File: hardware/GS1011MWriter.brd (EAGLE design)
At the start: 54.1 x 56 mm, 15 parts, among them IC1 SN74LVC2G125DCU, IC2 SN74LVC2G125DCU

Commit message: routing
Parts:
- removed $1_6_$, U$2: LED-SPACER, my:LED-SPACER
- removed STANDOFF1, STANDOFF2, STANDOFF3, STANDOFF4: STAND-OFF, my:STAND-OFF
- removed U$1: (no value), logo:IRKIT-LOGO
- moved R3 56.4 mm to (14.3, 16.9), turned to 180 degrees
- moved S1 53.1 mm to (20.9, 18.4), turned to 180 degrees
- moved CN1 47.0 mm to (3.70, 10.4)
- moved R1 41.1 mm to (21.4, 5.40), turned to 90 degrees
- moved R2 35.6 mm to (11.8, 4.80), turned to 90 degrees
- moved IC2 35.1 mm to (16.9, 6.60), turned to 90 degrees
- moved CN2 34.5 mm to (27.8, 9.80), turned to 90 degrees
- moved IC1 33.0 mm to (11.8, 13.6), turned to 270 degrees
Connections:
- net +3V3: now also CN1.1
- net GND: no longer CN1.1
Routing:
- net GND: track 119.4 -> 7.72 mm, vias 87 -> 1
- net +3V3: track 0.00 -> 27.8 mm
- net +5V: track 2.53 -> 29.4 mm, vias 0 -> 1
- net TXD: track 0.00 -> 23.4 mm, vias 0 -> 1
- net RTS#: track 0.00 -> 15.5 mm
- net WIFI_UART0_RX: track 12.9 -> 0.00 mm
- net N$1: track 0.00 -> 10.1 mm
- net WIFI_UART0_RTS: track 15.2 -> 5.70 mm, vias 2 -> 0
- net WIFI_UART0_TX: track 18.4 -> 10.1 mm, vias 2 -> 1
- net WIFI_UART0_CTS: track 14.1 -> 15.5 mm
- net WIFI_UART1_RTS: track 28.4 -> 29.2 mm
- removed copper zone on layer 1, net GND
- removed copper zone on layer 16, net GND
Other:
- board size 54.1 x 56 mm -> 30 x 20 mm
- board text removed: "+5V"
- board text removed: "GND"
- board text removed: "IRKit v1.1.1"

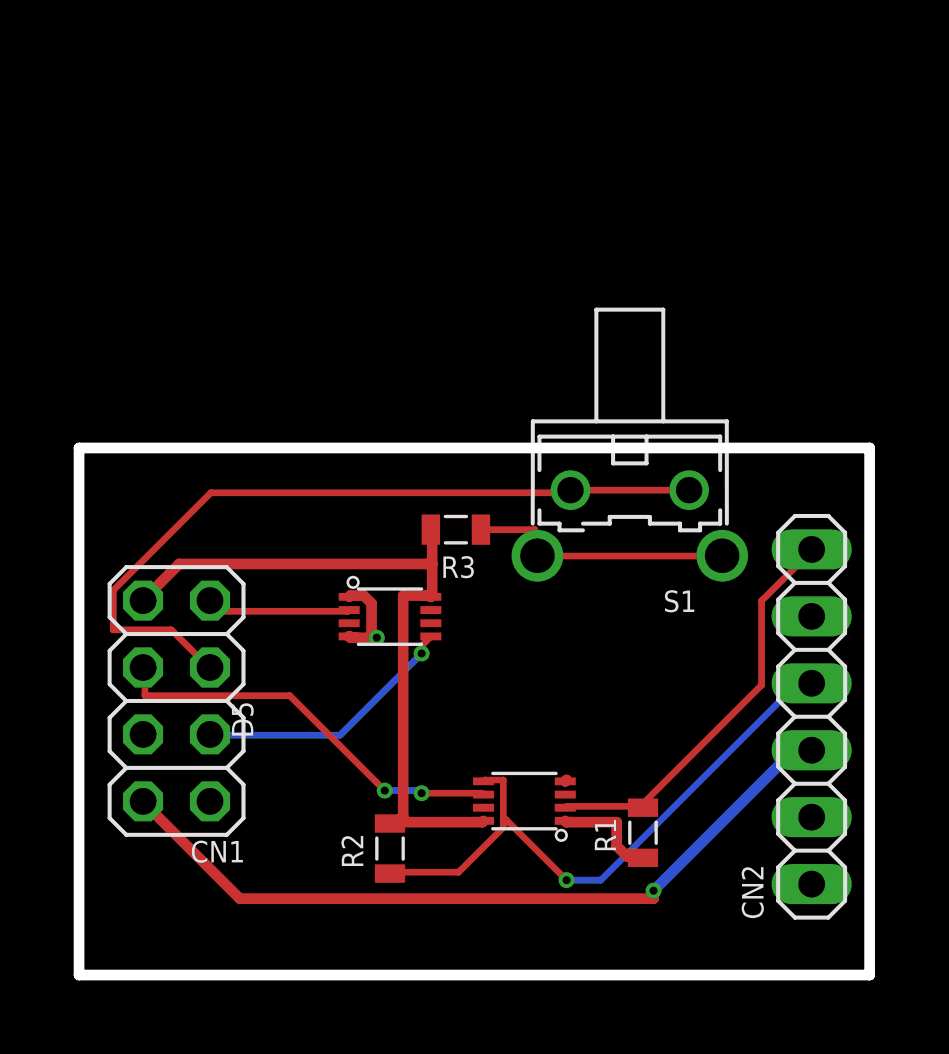
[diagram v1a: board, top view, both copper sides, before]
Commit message: routed GS1011MIPS writer
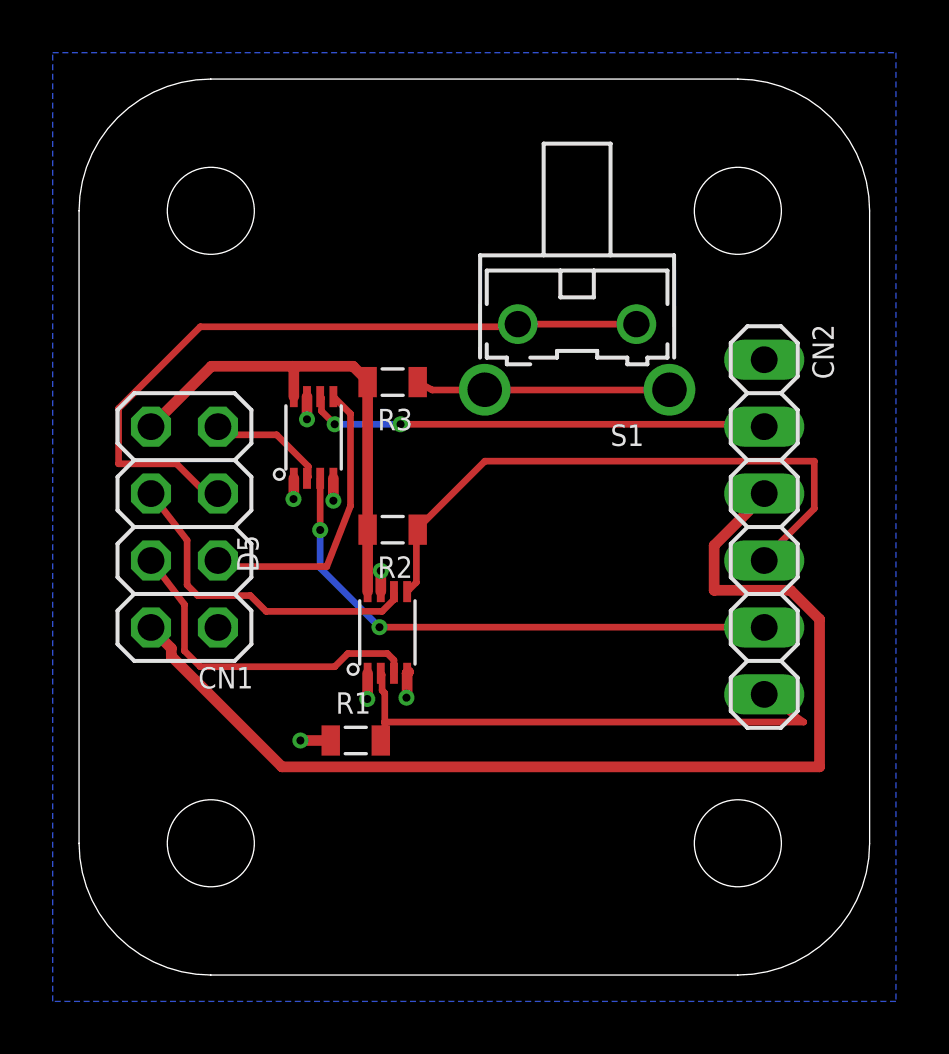
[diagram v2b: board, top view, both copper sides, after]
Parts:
- added STANDOFF1, STANDOFF2, STANDOFF3, STANDOFF4: STAND-OFF, my:STAND-OFF
- moved R2 12.1 mm to (11.9, 16.9), turned to 180 degrees
- moved R1 11.4 mm to (10.5, 8.90), turned to 0 degrees
- moved IC2 8.25 mm to (11.7, 13.0), turned to 0 degrees
- moved CN2 7.42 mm to (26.0, 17.0), turned to 270 degrees
- moved IC1 7.39 mm to (8.90, 20.4), turned to 0 degrees
- moved S1 6.61 mm to (18.9, 24.7)
- moved CN1 6.61 mm to (4.00, 17.0)
- moved R3 6.09 mm to (11.9, 22.5)
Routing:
- net RXD: track 0.00 -> 21.6 mm, vias 0 -> 2
- net CTS#: track 0.00 -> 17.7 mm, vias 0 -> 2
- net WIFI_UART0_RX: track 0.00 -> 12.9 mm
- net +5V: track 29.4 -> 42.3 mm, vias 1 -> 0
- net +3V3: track 27.8 -> 18.6 mm
- net RTS#: track 15.5 -> 20.4 mm
- net WIFI_UART0_CTS: track 15.5 -> 12.7 mm, vias 2 -> 0
- net WIFI_UART1_RTS: track 29.2 -> 27.6 mm
- net WIFI_UART0_TX: track 10.1 -> 11.3 mm, vias 1 -> 0
- net WIFI_UART0_RTS: track 5.70 -> 4.79 mm
- net GND: track 7.72 -> 6.81 mm, vias 1 -> 7
- net TXD: track 23.4 -> 23.2 mm, vias 1 -> 0
- added copper zone on layer 16, net GND
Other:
- board size 30 x 20 mm -> 30 x 34 mm

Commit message: I think I can directly connect TTL-232R-3V3's pins to GS1011MIPS's UART pins
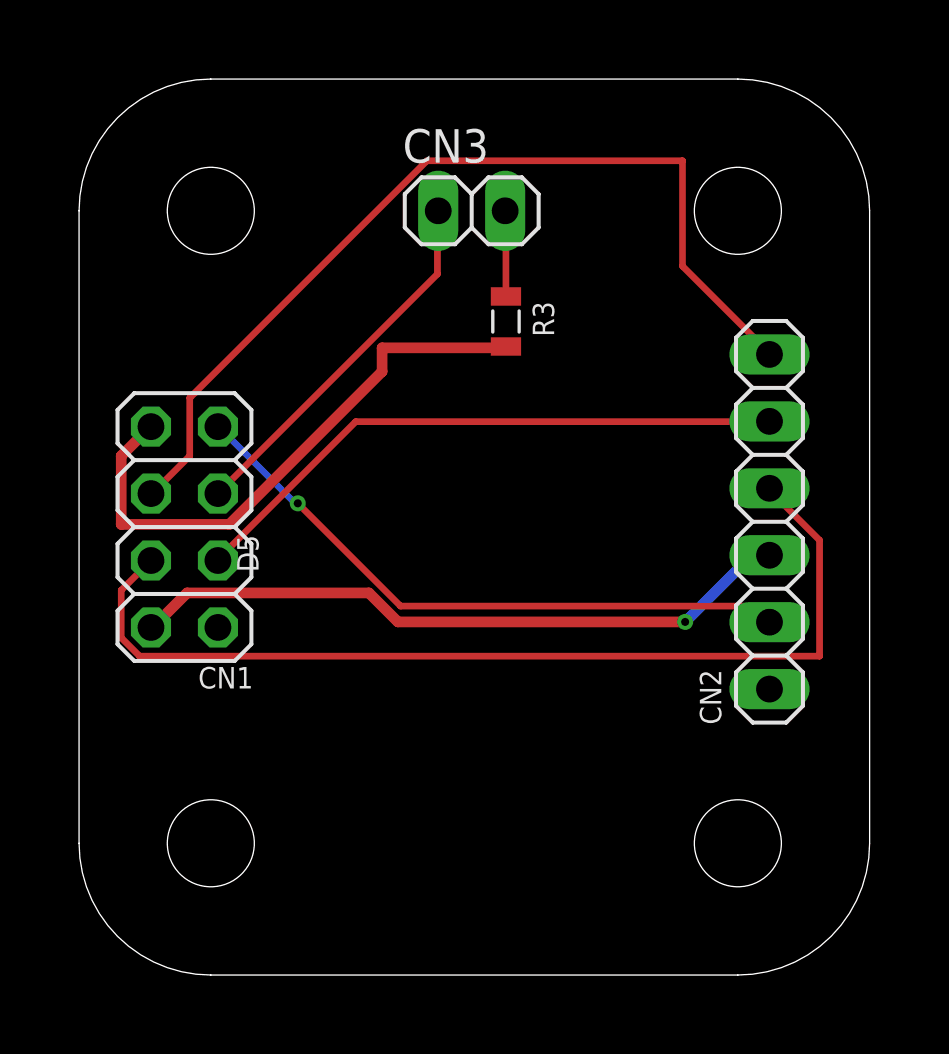
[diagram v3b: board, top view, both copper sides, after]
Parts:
- removed IC1, IC2: SN74LVC2G125DCU, my:VSSOP8
- removed R1, R2: 1M, my:2012
- removed S1: (no value), my:TACTILE-SWITCH-FSMRA6JH
- added CN3: (no value), pinhead:1X02
- R3: value 1k -> 10k
- moved R3 4.88 mm to (16.2, 24.8), turned to 270 degrees
- moved CN2 0.28 mm to (26.2, 17.2), turned to 90 degrees
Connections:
- removed net CTS#: CN2.2, IC1.6
- removed net RTS#: CN2.6, IC2.2, R1.2
- removed net RXD: CN2.5, IC1.3
- removed net TXD: CN2.4, IC2.5, R2.1
- net +3V3: no longer IC1.8, IC2.8, R2.2
- net GND: no longer IC1.1, IC1.4, IC1.7, IC2.1, IC2.4, IC2.7, R1.1
- net N$1: now also CN3.2; no longer S1.2@3, S1.2@4
- net WIFI_UART0_CTS: now also CN2.6; no longer IC2.6
- net WIFI_UART0_RTS: now also CN2.2; no longer IC1.2
- net WIFI_UART0_RX: now also CN2.4; no longer IC2.3
- net WIFI_UART0_TX: now also CN2.5; no longer IC1.5
- net WIFI_UART1_RTS: now also CN3.1; no longer S1.1@1, S1.1@2
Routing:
- net WIFI_UART0_RX: track 12.9 -> 37.3 mm
- net TXD: track 23.2 -> 0.00 mm
- net WIFI_UART0_CTS: track 12.7 -> 35.4 mm
- net RXD: track 21.6 -> 0.00 mm, vias 2 -> 0
- net RTS#: track 20.4 -> 0.00 mm
- net WIFI_UART0_RTS: track 4.79 -> 24.4 mm, vias 0 -> 1
- net CTS#: track 17.7 -> 0.00 mm, vias 2 -> 0
- net +5V: track 42.3 -> 25.5 mm, vias 0 -> 1
- net WIFI_UART1_RTS: track 27.6 -> 14.2 mm
- net WIFI_UART0_TX: track 11.3 -> 23.1 mm
- net GND: track 6.81 -> 0.00 mm, vias 7 -> 0
- net N$1: track 9.64 -> 3.28 mm
- net +3V3: track 18.6 -> 22.1 mm
- removed copper zone on layer 16, net GND
